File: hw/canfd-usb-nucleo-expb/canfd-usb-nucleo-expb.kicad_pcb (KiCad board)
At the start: 2 copper layers, 70 x 59 mm, 58 parts, among them CN1 POWER, CN2 CONN, J1 USB_C_Receptacle_USB2.0, J2 Conn_01x10, J3 Conn_01x10, J4 Conn_01x10, SW1 SW_Push_Dual_x2, SW2 SW_Push_Dual_x2, SW3 SW_Push_Dual_x2, U1 USBLC6-2SC6, U2 ATA6561-GAQW-N, U3 ATA6561-GAQW-N, U4 ATA6561-GAQW-N

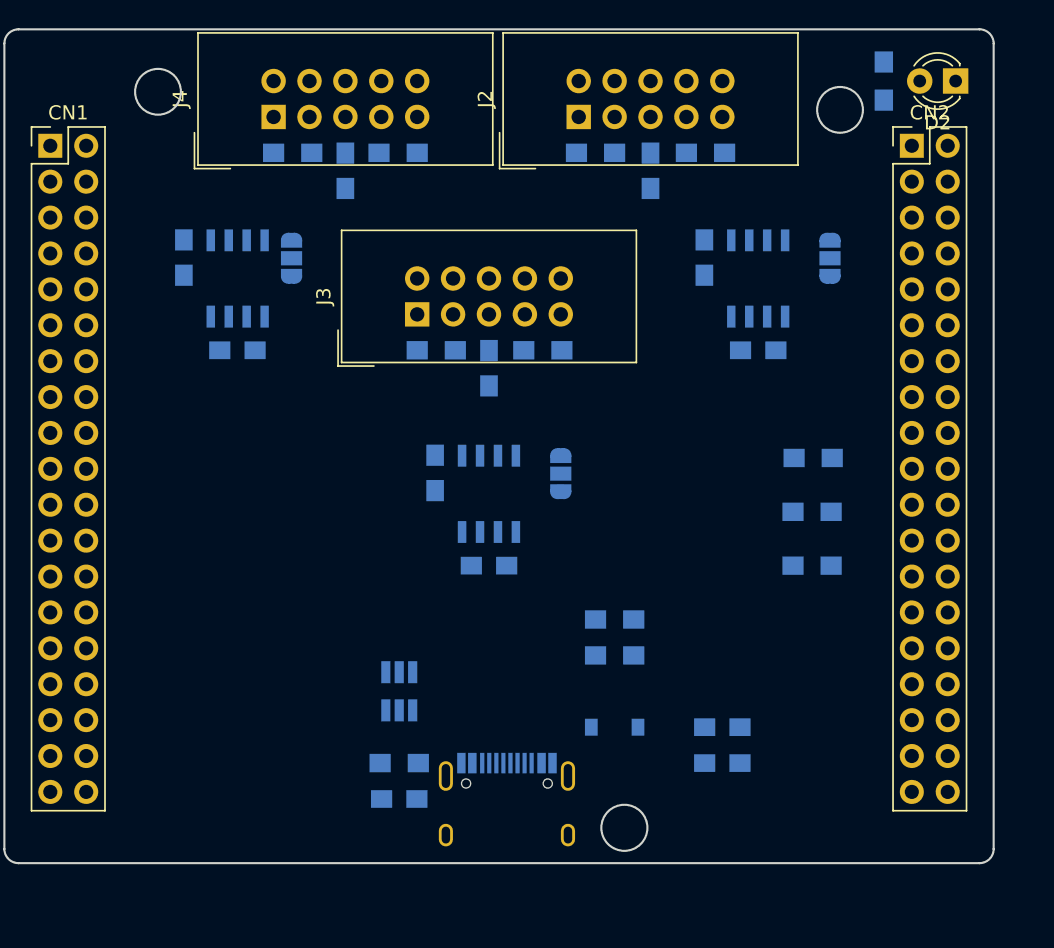
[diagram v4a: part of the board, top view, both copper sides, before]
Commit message: HW: PCB Layout: Part 1
Fixed the USBLC6-2SC6 part;
Routed most of the PHY can parts of the board.

Signed-off-by: AlexeyZ <silkt207@gmail.com>
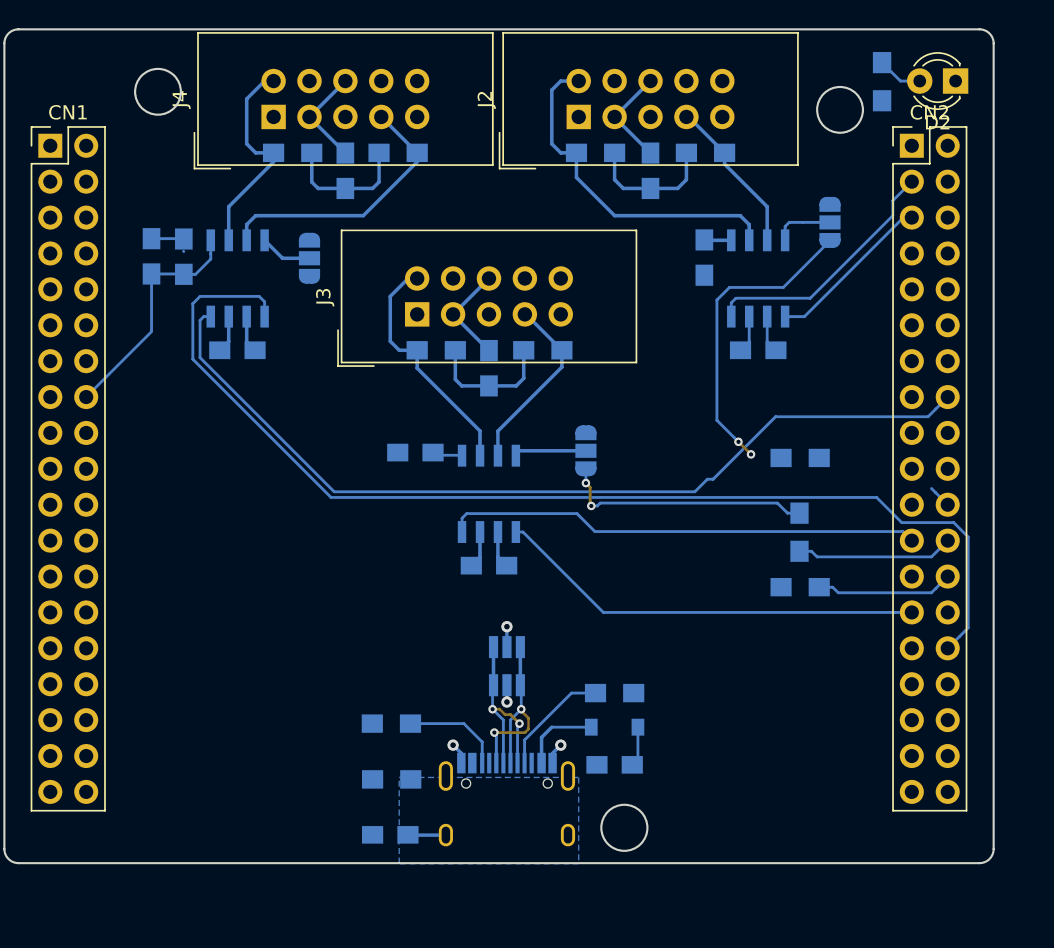
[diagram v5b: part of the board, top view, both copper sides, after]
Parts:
- moved C3 50.6 mm to (114.9, 86.0), turned to 90 degrees
- moved R5 16.5 mm to (129.6, 119.0), turned to 180 degrees
- moved U1 7.82 mm to (137.8, 114.9)
- moved C2 7.62 mm to (145.4, 121.9), turned to 180 degrees
- moved R6 5.21 mm to (145.4, 116.8)
- moved C1 2.62 mm to (129.5, 126.9)
- moved JP1 2.54 mm to (160.7, 83.5)
- moved JP2 2.40 mm to (143.4, 99.7)
- moved C12 2.29 mm to (112.6, 85.9), turned to 90 degrees
- moved C10 2.01 mm to (131.3, 99.8), turned to 180 degrees
- moved R4 1.74 mm to (158.5, 109.3)
- moved R3 1.70 mm to (158.5, 105.5), turned to 90 degrees
- moved R1 1.28 mm to (129.6, 123.0)
- moved JP3 1.27 mm to (123.8, 86.1), turned to 90 degrees
- moved R2 0.92 mm to (158.5, 100.2)
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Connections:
- net CAN1_H+ renamed CAN1_P
- net CAN1_L- renamed CAN1_N
- net CAN2_H+ renamed CAN2_P
- net CAN2_L+ renamed CAN2_N
- net CAN3_H+ renamed CAN3_P
- net CAN3_L- renamed CAN3_N
- CN2 pad 16: RX2 -> RX3
- CN2 pad 23: RX3 -> RX2
- CN2 pad 27: TX3 -> TX2
- CN2 pad 30: TX2 -> TX3
- J1 pad A8: (no net) -> Net-(J1-PadA8)
- J1 pad B8: (no net) -> Net-(J1-PadB8)
- U1 pad 3: (no net) -> D-
- U1 pad 4: (no net) -> D-
- U1 pad 6: D- -> D+
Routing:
- net TX3: track 0.00 -> 79.0 mm
- net RX3: track 0.00 -> 63.3 mm
- net GND: track 0.00 -> 36.0 mm, vias 0 -> 3
- net RX2: track 0.00 -> 33.7 mm
- net TX2: track 0.00 -> 30.4 mm
- net CAN1_N: track 0.00 -> 24.4 mm
- net STANDBY_1: track 0.00 -> 21.7 mm, vias 0 -> 2
- net +3V3: track 0.00 -> 20.4 mm
- net CAN3_P: track 0.00 -> 19.2 mm
- net RX1: track 0.00 -> 17.9 mm
- net STANDBY_2: track 0.00 -> 17.9 mm, vias 0 -> 2
- net CAN2_N: track 0.00 -> 17.1 mm
- net CAN3_N: track 0.00 -> 15.3 mm
- net D+: track 0.00 -> 15.2 mm, vias 0 -> 2
- net D-: track 0.00 -> 14.0 mm, vias 0 -> 2
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- added copper zone on B.Cu, net Net-(C1-Pad1)
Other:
- net class Default: trace_width 0.25 -> 0.2; via_dia 0.8 -> 0.6; via_drill 0.4 -> 0.3
- rule via_min_size: 0.4 -> 0.3

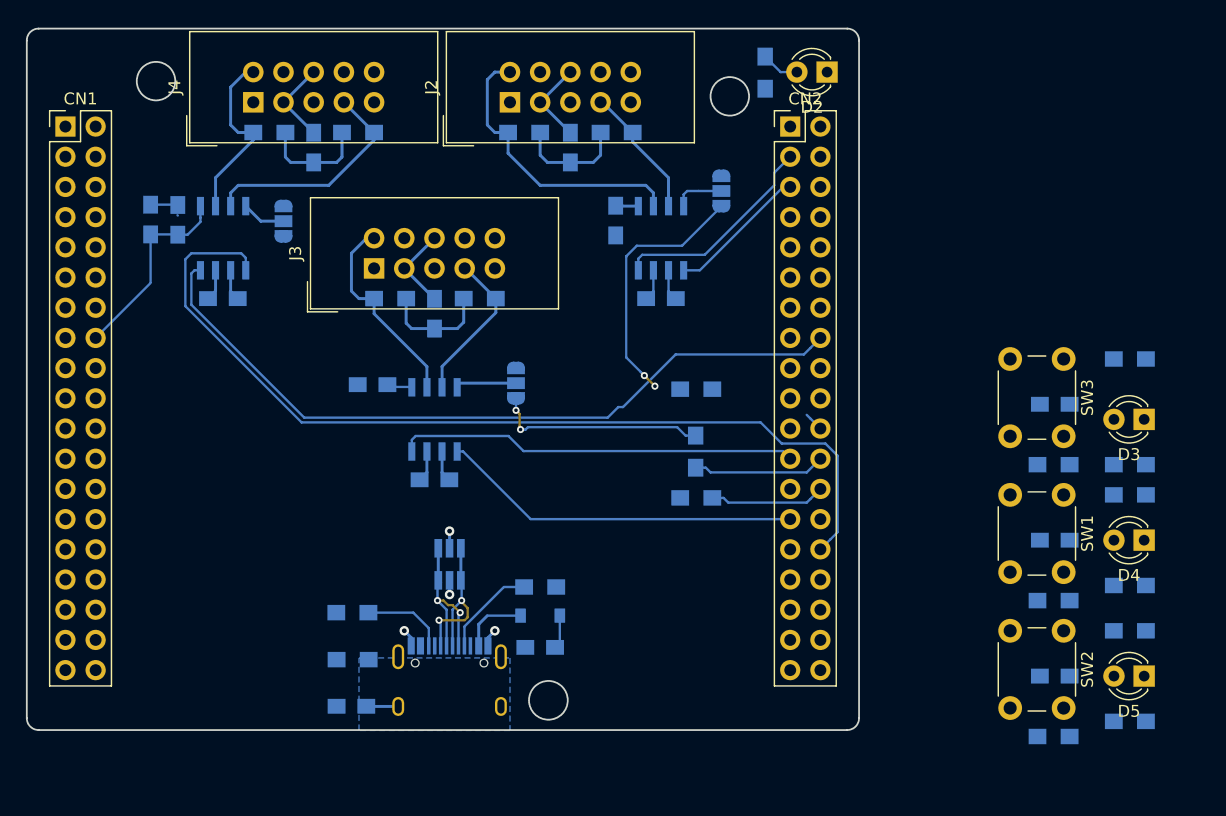
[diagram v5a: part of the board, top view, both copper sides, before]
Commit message: HW: PCB layout is ready to review
Co-authored-by: Viacheslav Olizarenko <stiwenss@gmail.com>
Co-authored-by: AlexeyZ <silkt207@gmail.com>
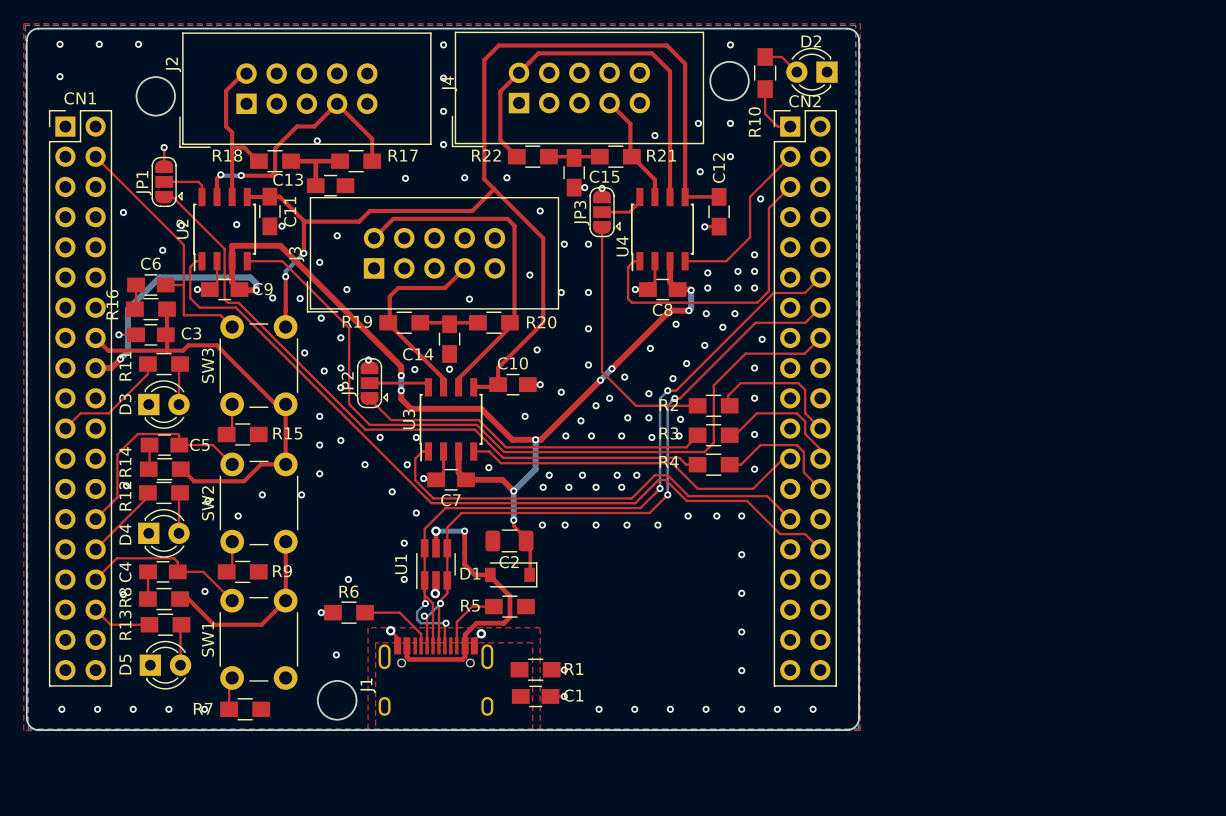
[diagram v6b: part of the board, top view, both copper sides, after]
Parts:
- C1, C10, C11, C12, C13, C14, C15, C3, C4, C5, C6, C7, C8, C9, D1, J1, JP1, JP2, JP3, R1, R10, R11, R12, R13, R14, R15, R16, R17, R18, R19, R2, R20, R21, R22, R3, R4, R5, R6, R7, R8, R9, U1, U2, U3, U4: moved to F.Cu
- C2: footprint Capacitors_SMD:C_0805_HandSoldering -> Capacitor_SMD:C_1206_3216Metric; moved to F.Cu
- CN1: value POWER -> Conn_02x19_Odd_Even
- moved D3 83.7 mm to (112.5, 101.5), turned to 0 degrees
- moved D4 83.7 mm to (112.5, 112.3), turned to 0 degrees
- moved D5 83.6 mm to (112.6, 123.4), turned to 0 degrees
- moved R16 82.4 mm to (112.7, 93.5), turned to 180 degrees
- moved R11 81.7 mm to (113.8, 98.1), turned to 0 degrees
- moved R12 81.6 mm to (113.8, 108.9), turned to 0 degrees
- moved R13 81.5 mm to (113.9, 120.0), turned to 0 degrees
- moved R8 81.3 mm to (113.8, 117.9), turned to 180 degrees
- moved R14 81.2 mm to (113.8, 106.9), turned to 180 degrees
- moved C5 77.4 mm to (113.8, 104.9), turned to 0 degrees
- moved C6 76.7 mm to (112.7, 91.4), turned to 0 degrees
- moved C4 75.1 mm to (113.7, 115.6), turned to 0 degrees
- moved SW1 71.6 mm to (119.5, 124.5), turned to 90 degrees
- moved SW2 70.3 mm to (119.5, 113.0), turned to 90 degrees
- moved SW3 70.0 mm to (119.5, 101.5), turned to 90 degrees
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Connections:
- net Net-(D1-Pad2) renamed /Vbus
- CN1 pad 21: (no net) -> LED2
- CN1 pad 28: (no net) -> SW2
- CN1 pad 30: (no net) -> LED3
- CN1 pad 32: (no net) -> SW1
- CN1 pad 34: (no net) -> LED4
- CN1 pad 4: (no net) -> SW3
- CN2 pad 1: SW1 -> LED1
- CN2 pad 16: RX3 -> RX1
- CN2 pad 18: LED1 -> (no net)
- CN2 pad 19: LED3 -> (no net)
- CN2 pad 2: SW2 -> (no net)
- CN2 pad 21: LED2 -> (no net)
- CN2 pad 3: RX1 -> RX3
- CN2 pad 30: TX3 -> TX1
- CN2 pad 33: LED4 -> (no net)
- CN2 pad 4: SW3 -> (no net)
- CN2 pad 5: TX1 -> TX3
- J1 pad A8: Net-(J1-PadA8) -> (no net)
- J1 pad B8: Net-(J1-PadB8) -> (no net)
- R2 pad 2: STANDBY_1 -> STANDBY_3
- R4 pad 2: STANDBY_3 -> STANDBY_1
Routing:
- net +3V3: track 20.4 -> 150.1 mm, vias 0 -> 2
- net +5V: track 10.7 -> 101.6 mm, vias 0 -> 11
- net TX1: track 11.9 -> 67.2 mm
- net TX3: track 79.0 -> 25.7 mm
- net D+: track 15.2 -> 64.4 mm, vias 2 -> 4
- net RX3: track 63.3 -> 14.5 mm
- net RX1: track 17.9 -> 65.4 mm
- net D-: track 14.0 -> 58.3 mm, vias 2 -> 4
- net STANDBY_1: track 21.7 -> 56.7 mm, vias 2 -> 0
- net SW3: track 0.00 -> 25.1 mm
- net SW2: track 0.00 -> 21.6 mm
- net STANDBY_3: track 0.00 -> 21.2 mm
- net /Vbus: track 7.08 -> 25.7 mm, vias 1 -> 2
- net CAN3_N: track 15.3 -> 32.9 mm
- net SW1: track 0.00 -> 16.9 mm
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- added copper zone on B.Cu, net GND
- added copper zone on F.Cu, net GND
- added copper zone on F.Cu, net Net-(C1-Pad1)
- removed copper zone on B.Cu, net Net-(C1-Pad1)
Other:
- outline, holes or cut-outs redrawn
- net class Default: trace_width 0.2 -> 0.3

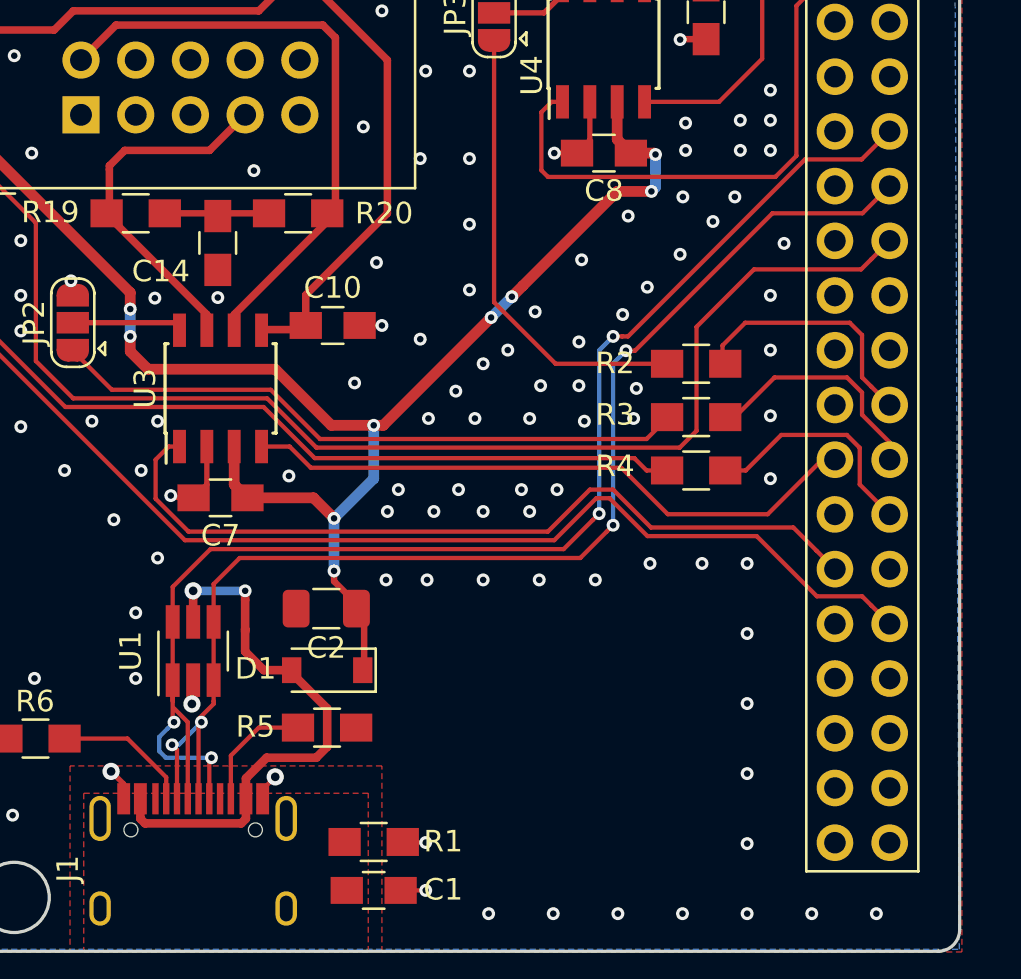
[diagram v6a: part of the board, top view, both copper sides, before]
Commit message: HW: USB routes are fixed
Signed-off-by: Viacheslav Olizarenko <stiwenss@gmail.com>
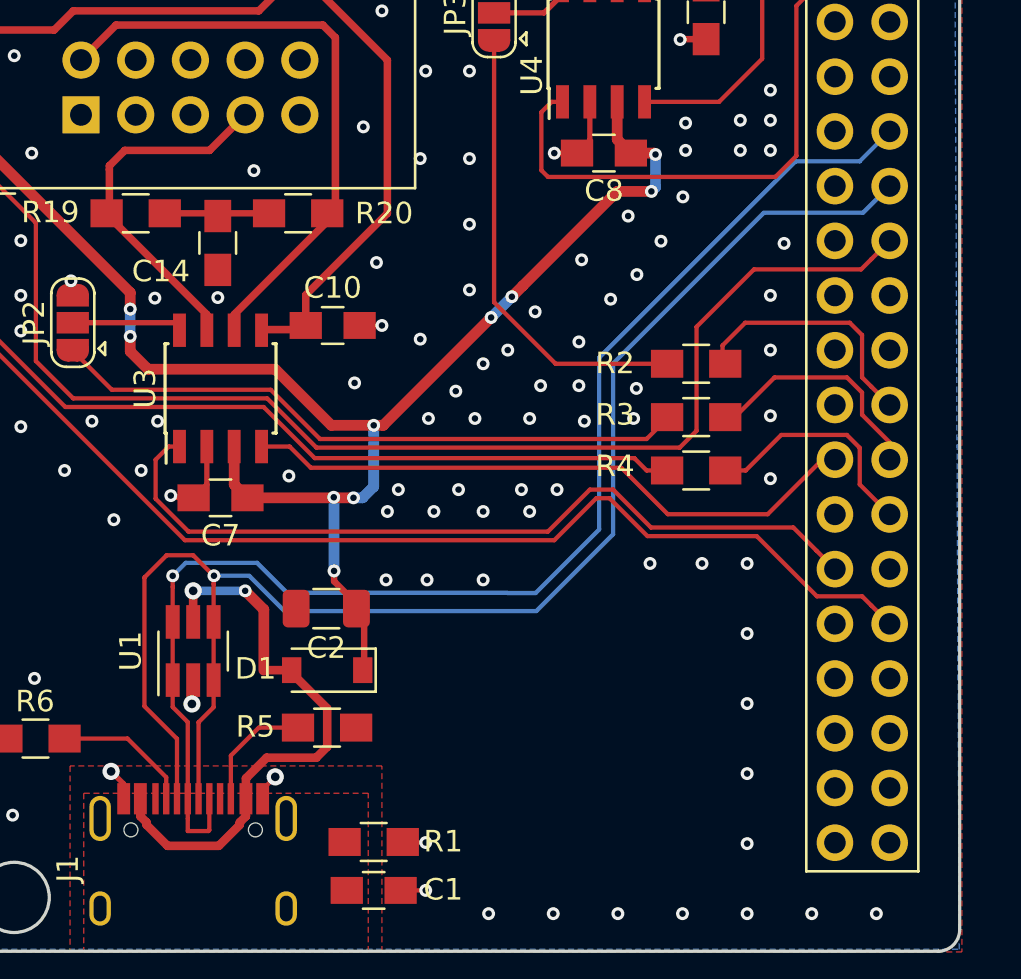
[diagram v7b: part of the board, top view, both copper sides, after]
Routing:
- net D-: track 58.3 -> 70.5 mm, vias 4 -> 1
- net D+: track 64.4 -> 62.3 mm, vias 4 -> 1
- net /Vbus: track 25.7 -> 26.5 mm
- net +5V: track 101.6 -> 102.0 mm, vias 11 -> 12
- net GND: vias 146 -> 139
